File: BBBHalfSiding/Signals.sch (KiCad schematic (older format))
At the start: 10 parts, among them J1 Address, T1 Signals A, B, T2 Signals C, D, U1 MCP23017, U2 ULN2803A, U3 ULN2803A

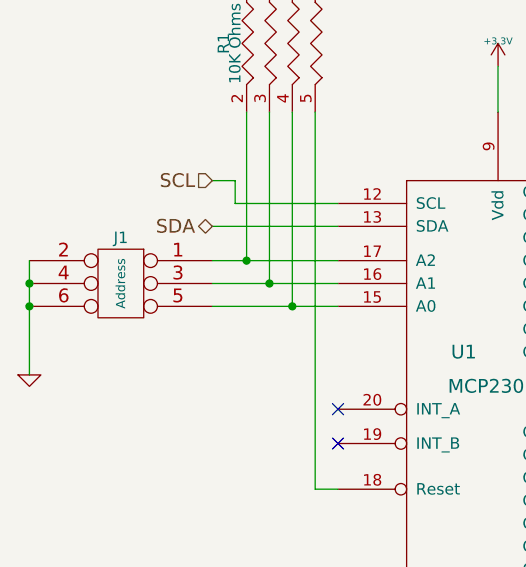
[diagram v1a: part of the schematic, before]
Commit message: Updates to BBBHalfSiding (silk screen tweaks)
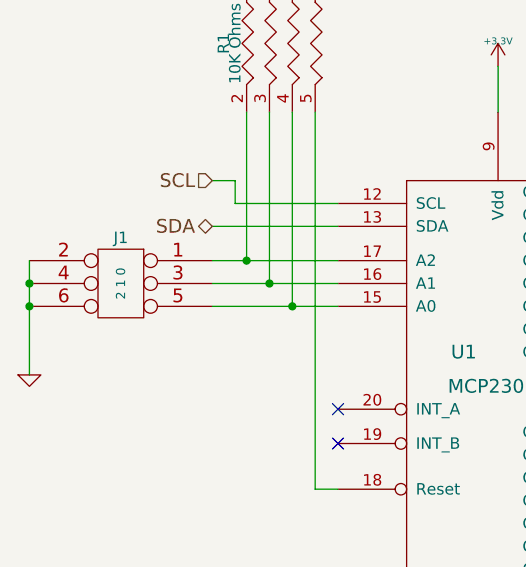
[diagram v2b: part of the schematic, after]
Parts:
- J1: value Address -> 2 1 0
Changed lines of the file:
@@
 Sheet 3 4
 Title ""
-Date "19 oct 2018"
+Date "20 oct 2018"
 Rev ""
 Comp ""
@@
 P 1900 2500
 F 0 "J1" H 1900 2750 50  0000 C CNN
-F 1 "Address" V 1900 2550 40  0000 C CNN
+F 1 "2  1  0" V 1900 2550 40  0000 C CNN
 F 2 "~" H 1900 2500 60  0000 C CNN
 F 3 "~" H 1900 2500 60  0000 C CNN

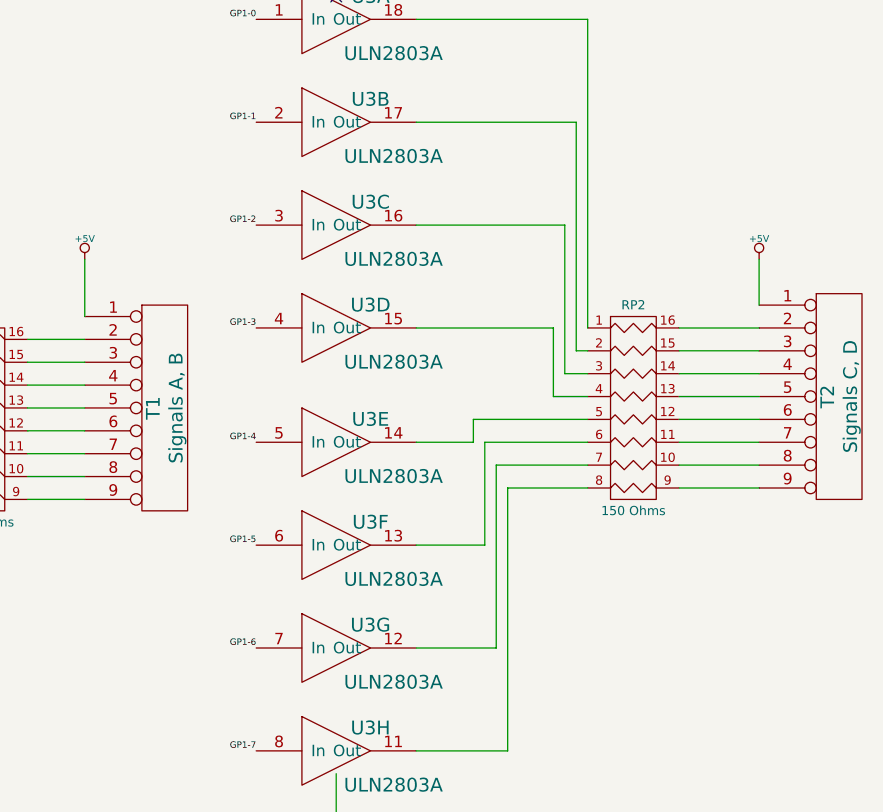
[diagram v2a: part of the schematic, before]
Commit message: Add missing bypass caps.
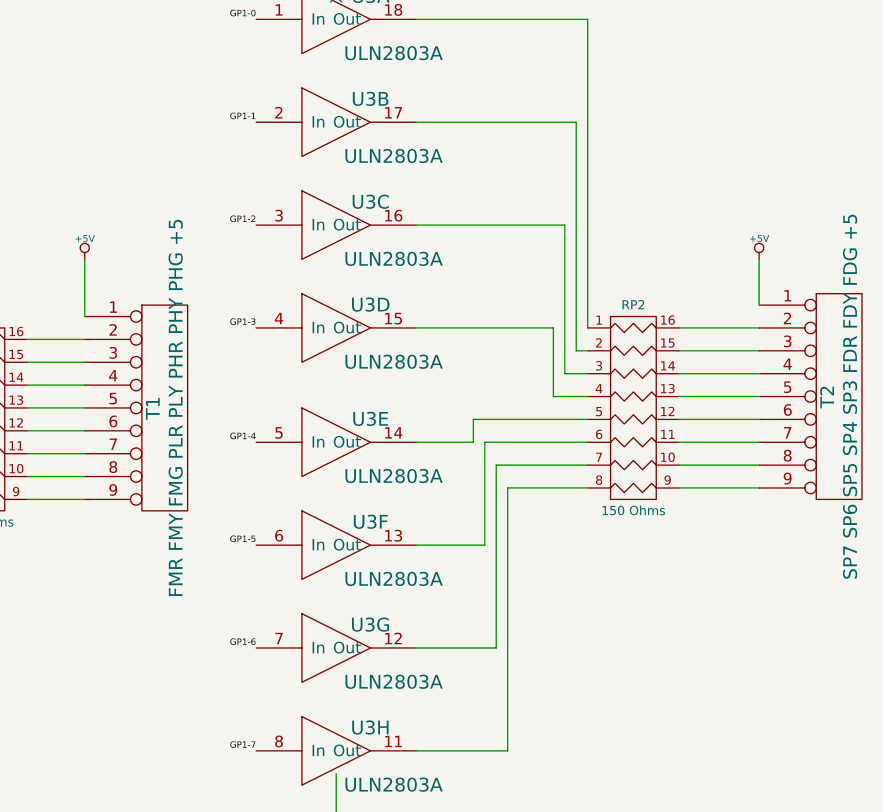
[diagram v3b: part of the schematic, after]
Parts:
- T1: value Signals A, B -> FMR FMY FMG PLR PLY PHR PHY PHG +5
- T2: value Signals C, D -> SP7 SP6 SP5 SP4 SP3 FDR FDY FDG +5
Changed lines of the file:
@@
 $EndComp
 $Comp
-L +3.3V #PWR045
+L +3.3V #PWR047
 U 1 1 5BBB75A2
 P 3550 1500
-F 0 "#PWR045" H 3550 1460 30  0001 C CNN
+F 0 "#PWR047" H 3550 1460 30  0001 C CNN
 F 1 "+3.3V" H 3550 1610 30  0000 C CNN
 F 2 "" H 3550 1500 60  0000 C CNN
@@
 $EndComp
 $Comp
-L GND #PWR046
+L GND #PWR048
 U 1 1 5BBB75B1
 P 3450 4400
-F 0 "#PWR046" H 3450 4400 30  0001 C CNN
+F 0 "#PWR048" H 3450 4400 30  0001 C CNN
 F 1 "GND" H 3450 4330 30  0001 C CNN
 F 2 "" H 3450 4400 60  0000 C CNN
@@
 $EndComp
 $Comp
-L GND #PWR047
+L GND #PWR049
 U 1 1 5BBB75C0
 P 5700 5700
-F 0 "#PWR047" H 5700 5700 30  0001 C CNN
+F 0 "#PWR049" H 5700 5700 30  0001 C CNN
 F 1 "GND" H 5700 5630 30  0001 C CNN
 F 2 "" H 5700 5700 60  0000 C CNN
@@
 $EndComp
 $Comp
-L GND #PWR048
+L GND #PWR050
 U 1 1 5BBB75CF
 P 8250 5700
-F 0 "#PWR048" H 8250 5700 30  0001 C CNN
+F 0 "#PWR050" H 8250 5700 30  0001 C CNN
 F 1 "GND" H 8250 5630 30  0001 C CNN
 F 2 "" H 8250 5700 60  0000 C CNN
@@
 $EndComp
 $Comp
-L GND #PWR049
+L GND #PWR051
 U 1 1 5BBB75DE
 P 1500 2850
-F 0 "#PWR049" H 1500 2850 30  0001 C CNN
+F 0 "#PWR051" H 1500 2850 30  0001 C CNN
 F 1 "GND" H 1500 2780 30  0001 C CNN
 F 2 "" H 1500 2850 60  0000 C CNN
@@
 P 7500 3800
 F 0 "T1" V 7450 3800 60  0000 C CNN
-F 1 "Signals A, B" V 7550 3800 60  0000 C CNN
+F 1 "FMR FMY FMG PLR PLY PHR PHY PHG +5" V 7550 3800 60  0000 C CNN
 F 2 "~" H 7500 3800 60  0000 C CNN
 F 3 "~" H 7500 3800 60  0000 C CNN
@@
 P 10450 3750
 F 0 "T2" V 10400 3750 60  0000 C CNN
-F 1 "Signals C, D" V 10500 3750 60  0000 C CNN
+F 1 "SP7 SP6 SP5 SP4 SP3 FDR FDY FDG +5" V 10500 3750 60  0000 C CNN
 F 2 "~" H 10450 3750 60  0000 C CNN
 F 3 "~" H 10450 3750 60  0000 C CNN
@@
 $EndComp
 $Comp
-L +5V #PWR050
+L +5V #PWR052
 U 1 1 5BBB7648
 P 7150 3150
-F 0 "#PWR050" H 7150 3240 20  0001 C CNN
+F 0 "#PWR052" H 7150 3240 20  0001 C CNN
 F 1 "+5V" H 7150 3240 30  0000 C CNN
 F 2 "" H 7150 3150 60  0000 C CNN
@@
 $EndComp
 $Comp
-L +5V #PWR051
+L +5V #PWR053
 U 1 1 5BBB7657
 P 10100 3150
-F 0 "#PWR051" H 10100 3240 20  0001 C CNN
+F 0 "#PWR053" H 10100 3240 20  0001 C CNN
 F 1 "+5V" H 10100 3240 30  0000 C CNN
 F 2 "" H 10100 3150 60  0000 C CNN
@@
 $EndComp
 $Comp
-L +3.3V #PWR052
+L +3.3V #PWR054
 U 1 1 5BBB7666
 P 4650 950
-F 0 "#PWR052" H 4650 910 30  0001 C CNN
+F 0 "#PWR054" H 4650 910 30  0001 C CNN
 F 1 "+3.3V" H 4650 1060 30  0000 C CNN
 F 2 "" H 4650 950 60  0000 C CNN
@@
 $EndComp
 $Comp
-L GND #PWR053
+L GND #PWR055
 U 1 1 5BBB7684
 P 4650 1850
-F 0 "#PWR053" H 4650 1850 30  0001 C CNN
+F 0 "#PWR055" H 4650 1850 30  0001 C CNN
 F 1 "GND" H 4650 1780 30  0001 C CNN
 F 2 "" H 4650 1850 60  0000 C CNN
@@
 	2300 2550 2850 2550
 $Comp
-L +3.3V #PWR054
+L +3.3V #PWR056
 U 1 1 5BBB76B2
 P 2600 950
-F 0 "#PWR054" H 2600 910 30  0001 C CNN
+F 0 "#PWR056" H 2600 910 30  0001 C CNN
 F 1 "+3.3V" H 2600 1060 30  0000 C CNN
 F 2 "" H 2600 950 60  0000 C CNN
